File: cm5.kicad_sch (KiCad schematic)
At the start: 25 parts, among them J11 JST_SH_1x4_BM04B-SRSS-TB-LF-SN, J2 CM5_1-100_3mm-stack, J3 CM5_101-200_3mm-stack, J4 JST_SH_1x3_BM03B-SRSS-TB-LF-SN, SW1 SW_TL2243

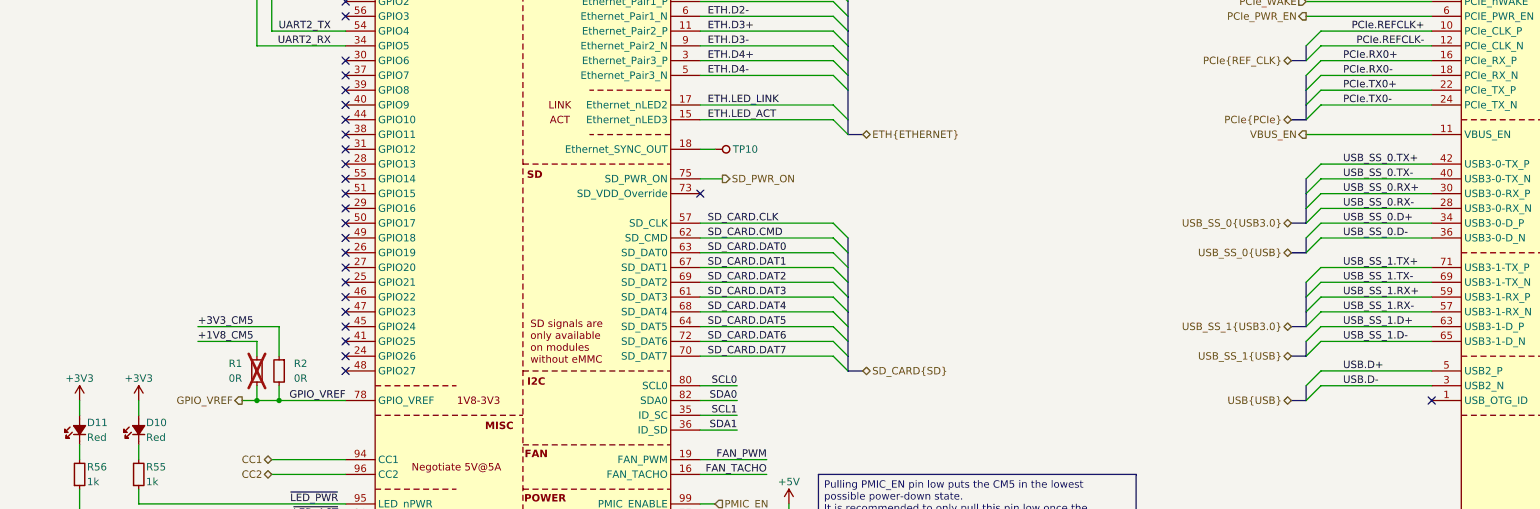
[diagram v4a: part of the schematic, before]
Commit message: [#1] Add USB to CAN schematic, add power flags to 5V and 3V3
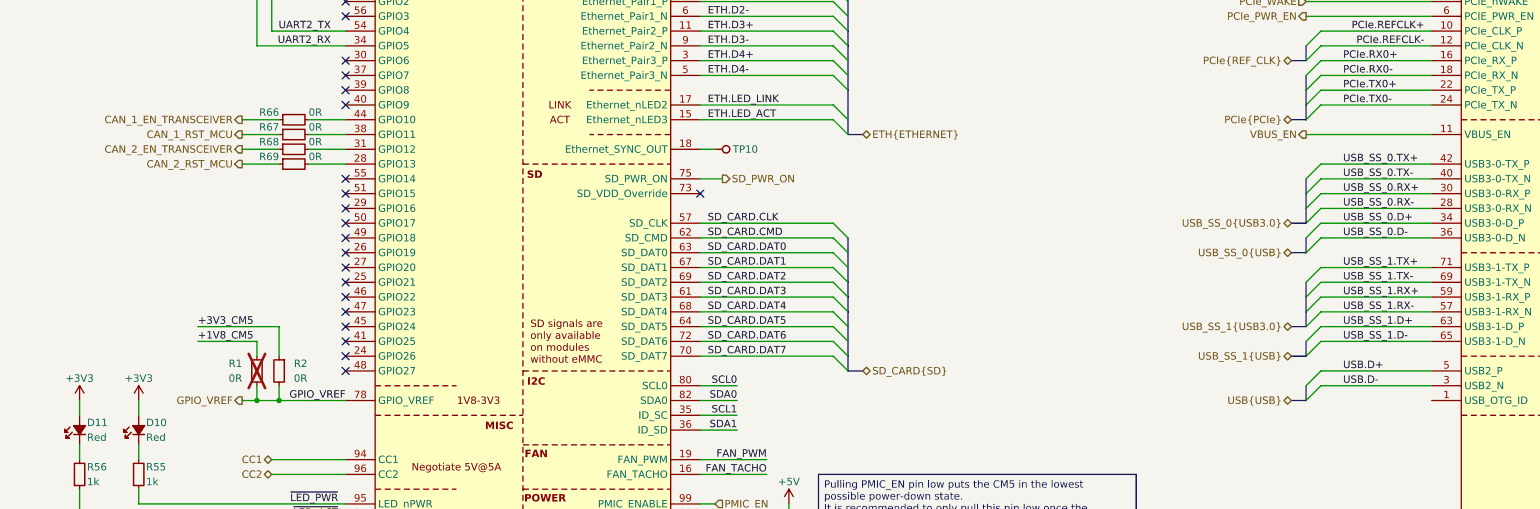
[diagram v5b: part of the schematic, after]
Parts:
- added R66, R67, R68, R69: R-0R-0402, DW-footprints:R_0402_1005Metric, symbol DW-resistors:R-0R-0402
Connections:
- net at J2.28 (GPIO13): now also R69.2
- net at J2.31 (GPIO12): now also R68.2
- net at J2.38 (GPIO11): now also R67.2
- net at J2.44 (GPIO10): now also R66.2
- new net CAN_1_EN_TRANSCEIVER: R66.1
- new net CAN_1_RST_MCU: R67.1
- new net CAN_2_EN_TRANSCEIVER: R68.1
- new net CAN_2_RST_MCU: R69.1
- no-connect marks 28 -> 23

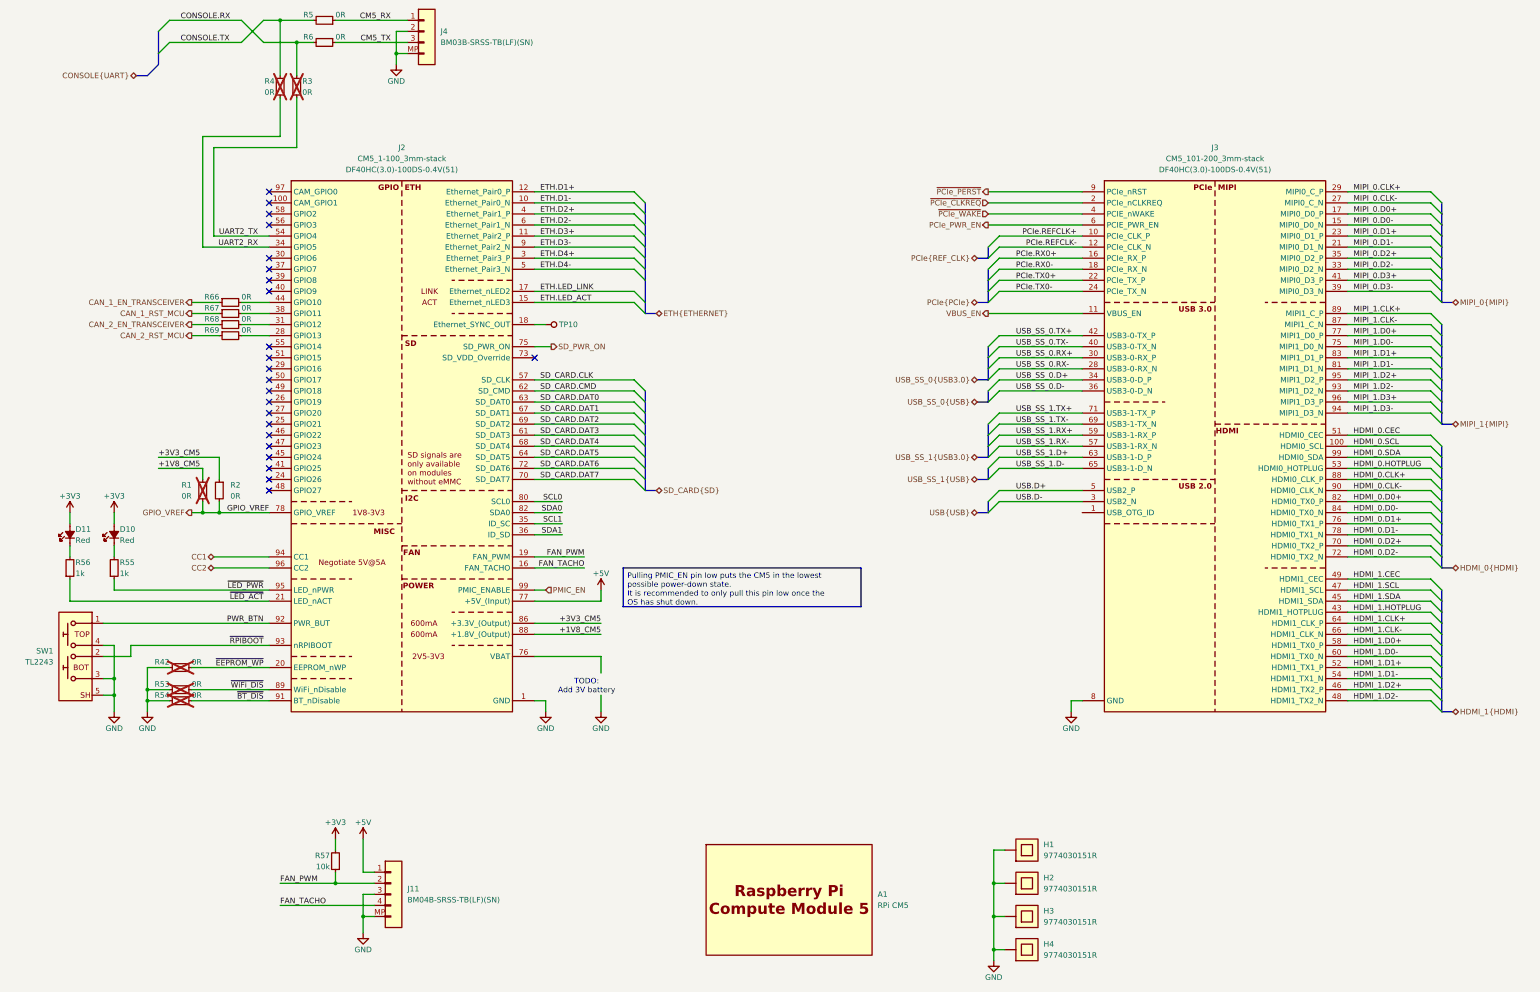
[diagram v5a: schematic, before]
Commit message: [#3] WIP: Clear ERC, re-annotate schematic
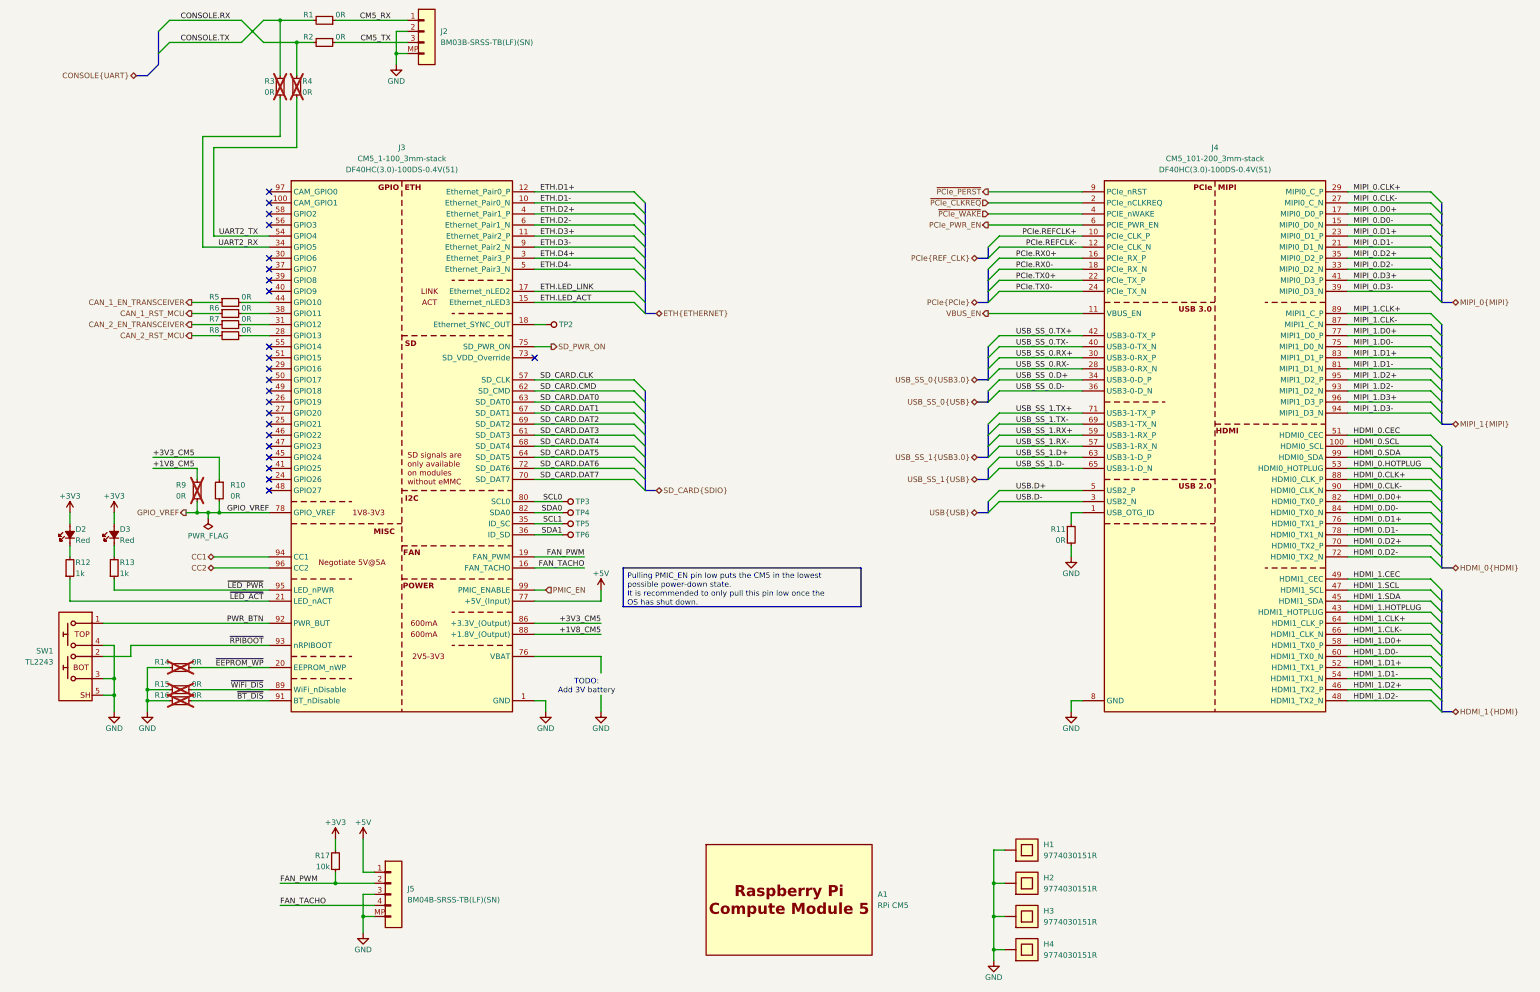
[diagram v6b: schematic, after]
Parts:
- added R11: R-0R-0402, DW-footprints:R_0402_1005Metric, symbol DW-resistors:R-0R-0402
- added TP3, TP4, TP5, TP6: TP_SMD_0.75mm, DW-footprints:TP_SMD_0.75mm, symbol DW-test-points:TP_SMD_0.75mm
- A1: symbol DW-SoM:CM5 -> DW-mechanical:CM5
- renumbered D11 to D2, D10 to D3, J4 to J2, J2 to J3, J3 to J4, J11 to J5, R5 to R1, R2 to R10, R56 to R12, R55 to R13, R42 to R14, R53 to R15, R54 to R16, R57 to R17, R6 to R2, R4 to R3, R3 to R4, R66 to R5, R67 to R6, R68 to R7, R69 to R8, R1 to R9, TP10 to TP2
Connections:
- net GND: now also R11.2
- net SCL0: now also TP3.1
- net SCL1: now also TP5.1
- net SDA0: now also TP4.1
- net SDA1: now also TP6.1
- net at J4.1 (USB_OTG_ID): now also R11.1
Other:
- moved on the sheet: R9

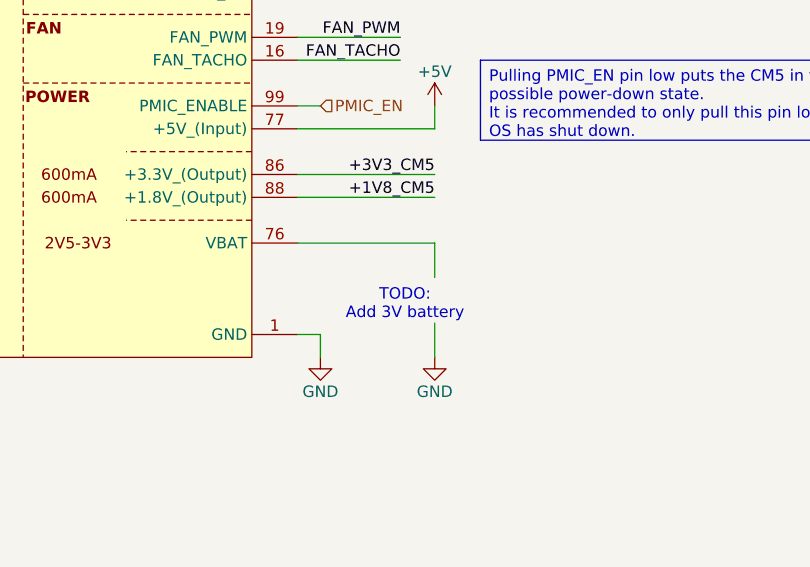
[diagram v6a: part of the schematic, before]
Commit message: [#3] Add CM5 RTC battery
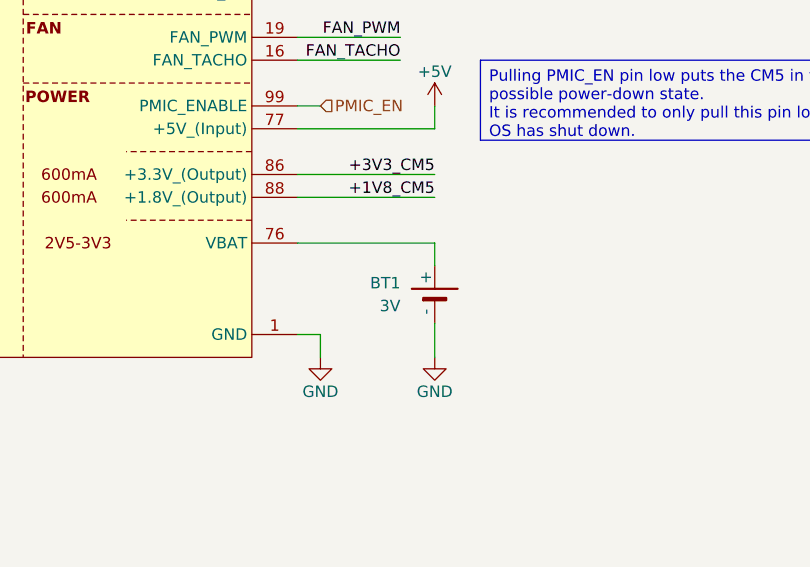
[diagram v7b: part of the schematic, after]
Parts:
- added BT1: Battery_MS621FE-FL11E, DW-footprints:Battery_MS621FE-FL11E, symbol DW-mechanical:Battery_MS621FE-FL11E
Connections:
- net GND: now also BT1.2 (-)
- net at J3.76 (VBAT): now also BT1.1 (+)
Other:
- note removed: "TODO: Add 3V battery"
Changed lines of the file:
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@@
 		)
 	)
-	(text "TODO:\nAdd 3V battery"
-		(exclude_from_sim no)
-		(at 149.098 201.168 0)
-		(effects
-			(font
-				(size 1.27 1.27)
-			)
-		)
-	)
 	(text_box "Pulling PMIC_EN pin low puts the CM5 in the lowest possible power-down state.\nIt is recommended to only pull this pin low once the OS has shut down."
 		(exclude_from_sim no)
@@
 		)
 	)
-	(wire
-		(pts
-			(xy 152.4 203.2) (xy 152.4 207.01)
-		)
-		(stroke
-			(width 0)
-			(type default)
-		)
-	)
 	(bus
 		(pts
@@
 	(wire
 		(pts
+			(xy 152.4 203.2) (xy 152.4 207.01)
+		)
+		(stroke
+			(width 0)
+			(type default)
+		)
+	)
+	(wire
+		(pts
 			(xy 323.85 151.13) (xy 342.9 151.13)
 		)
@@
 	(wire
 		(pts
-			(xy 152.4 194.31) (xy 152.4 198.12)
+			(xy 152.4 194.31) (xy 152.4 196.85)
 		)
 		(stroke
@@
 					(unit 1)
 				)
+			)
+		)
+	)
+	(symbol
+		(lib_id "DW-mechanical:Battery_MS621FE-FL11E")
+		(at 152.4 196.85 0)
+		(unit 1)
+		(exclude_from_sim no)
+		(in_bom yes)
+		(on_board yes)
+		(dnp no)
+		(fields_autoplaced yes)
+		(property "Reference" "BT1"
+			(at 148.59 198.755 0)
+			(effects
+				(font
+					(size 1.27 1.27)
+					(thickness 0.15)
+				)
+				(justify right)
+			)
+		)
+		(property "Value" "Battery_MS621FE-FL11E"
+			(at 157.48 199.39 0)
+			(effects
+				(font
+					(size 1.27 1.27)
+					(thickness 0.15)
+				)
+				(justify left bottom)
+				(hide yes)
+			)
+		)
+		(property "Footprint" "DW-footprints:Battery_MS621FE-FL11E"
+			(at 157.48 201.93 0)
+			(effects
+				(font
+					(size 1.27 1.27)
+					(thickness 0.15)
+				)
+				(justify left bottom)
+				(hide yes)
+			)
+		)
+		(property "Datasheet" "https://www.sii.co.jp/en/me/datasheets/ms-rechargeable/ms621fe/"
+			(at 157.48 204.47 0)
+			(effects
+				(font
+					(size 1.27 1.27)
+					(thickness 0.15)
+				)
+				(justify left bottom)
+				(hide yes)
+			)
+		)
+		(property "Description" "Rechargeable Battery, Coin Cell, Single Cell, 3 V, Lithium Manganese Dioxide, 5.5 mAh, Button Cell"
+			(at 157.48 207.01 0)
+			(effects
+				(font
+					(size 1.27 1.27)
+					(thickness 0.15)
+				)
+				(justify left bottom)
+				(hide yes)
+			)
+		)
+		(property "Manufacturer" "Seiko Instruments"
+			(at 157.48 209.55 0)
+			(effects
+				(font
+					(size 1.27 1.27)
+					(thickness 0.15)
+				)
+				(justify left bottom)
+				(hide yes)
+			)
+		)
+		(property "MPN" "MS621FE-FL11E"
+			(at 157.48 212.09 0)
+			(effects
+				(font
+					(size 1.27 1.27)
+					(thickness 0.15)
+				)
+				(justify left bottom)
+				(hide yes)
+			)
+		)
+		(property "Voltage" "3V"
+			(at 148.59 201.295 0)
+			(effects
+				(font
+					(size 1.27 1.27)
+					(thickness 0.15)
+				)
+				(justify right)
+			)
+		)
+		(pin "1"
+		)
+		(pin "2"
+		)
+		(instances
+			(project ""
+				(path "/090a8e41-87a8-4fb1-998b-60a2c0dc4cee/dfbce24a-51ce-450d-9d41-776080287e8b"
+					(reference "BT1")
+					(unit 1)
+				)

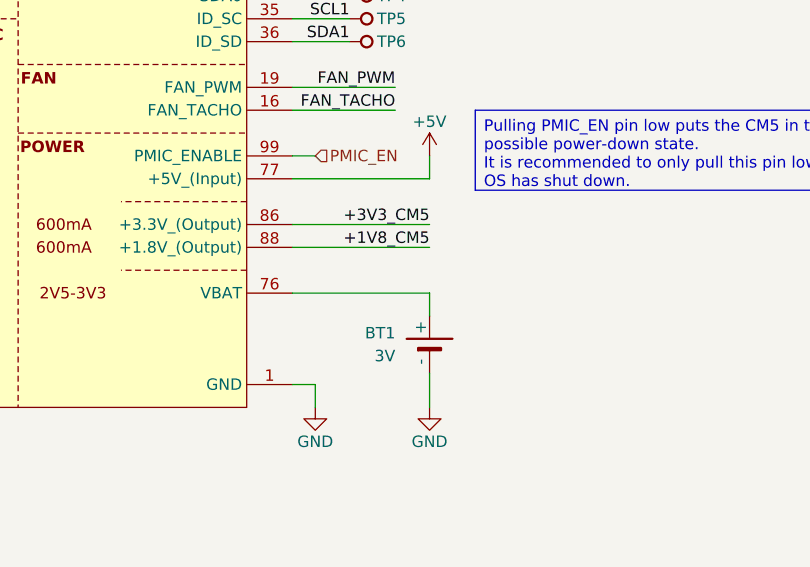
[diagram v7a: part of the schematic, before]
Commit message: [#3] Layout M.2 power
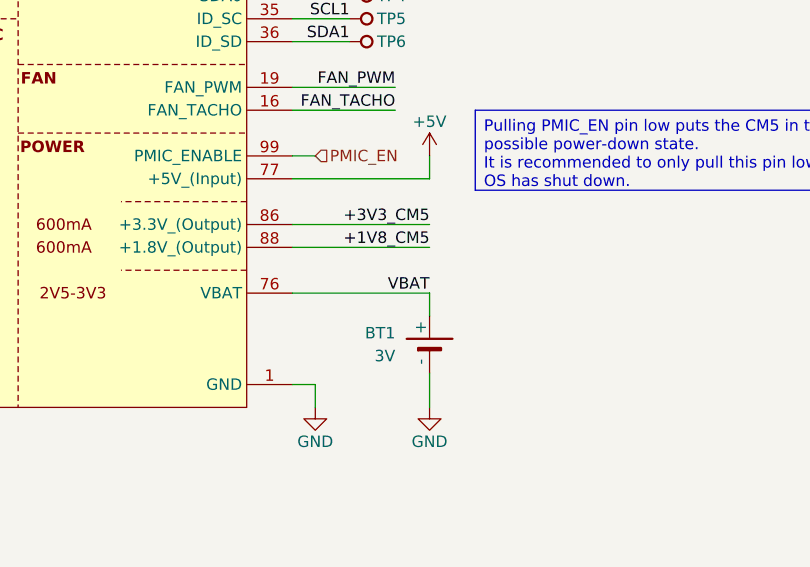
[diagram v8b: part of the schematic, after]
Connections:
- net VBAT: now reaches BT1.1 (+), J3.76 (VBAT)
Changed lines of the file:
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@@
+	(wire
+		(pts
+			(xy 137.16 194.31) (xy 152.4 194.31)
+		)
+		(stroke
+			(width 0)
+			(type default)
+		)
+	)
 	(wire
 		(pts
@@
 		(pts
 			(xy 82.55 53.34) (xy 86.36 53.34)
-		)
-		(stroke
-			(width 0)
-			(type default)
-		)
-	)
-	(wire
-		(pts
-			(xy 137.16 194.31) (xy 152.4 194.31)
 		)
 		(stroke
@@
 		)
 	)
+	(label "VBAT"
+		(at 152.4 194.31 180)
+		(effects
+			(font
+				(size 1.27 1.27)
+			)
+			(justify right bottom)
+		)
+	)
